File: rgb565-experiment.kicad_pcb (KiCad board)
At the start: 4 copper layers, 99.1 x 63.5 mm, 36 parts, among them J1 ST_SHIFTER_SOCKET, J2 Conn_01x02, SW1 SW_SPDT, U1 74HC00, U2 ST_SHIFTER, U3 ST_SHIFTER, U4 74HC245, U5 74LS257, U6 74HC245

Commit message: prepare next version
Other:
- board text added: "Original project : https://github.com/sporniket/atari-st-mod-rgb565-experiment v1.0.0-xprc3"
- board text removed: "Original project : https://github.com/sporniket/atari-st-mod-rgb565-experiment v1.0.0-xprc2"
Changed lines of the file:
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@@
   (page A4)
   (title_block
-    (title "Experimental RGB-565 mod for the Atari ST")
-    (date 2021-12-18)
-    (rev v1.0.0-xprc2)
+    (title "Experimental RGB-565 colorspace for the Atari ST")
+    (date 2021-12-24)
+    (rev v1.0.0-xprc3)
     (company Sporniket-Studio.com)
   )
@@
     (effects (font (size 1 1) (thickness 0.15)) (justify mirror))
   )
-  (gr_text "Original project : https://github.com/sporniket/atari-st-mod-rgb565-experiment v1.0.0-xprc2" (at 139.4206 132.0292) (layer F.SilkS)
+  (gr_text "Original project : https://github.com/sporniket/atari-st-mod-rgb565-experiment v1.0.0-xprc3" (at 139.4206 132.0292) (layer F.SilkS)
     (effects (font (size 1.016 1.016) (thickness 0.1524)))
   )

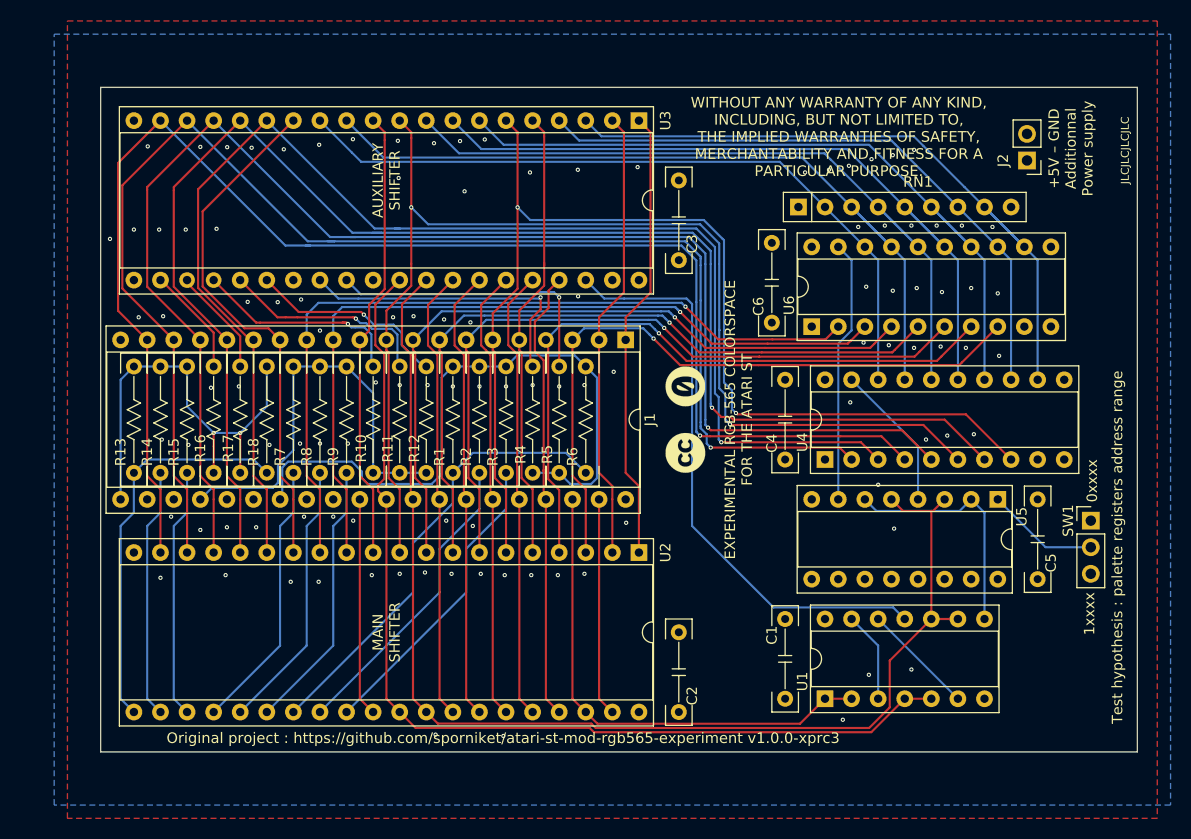
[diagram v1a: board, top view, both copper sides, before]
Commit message: Release Candidate 1 : modifications following experiments with the experimental version
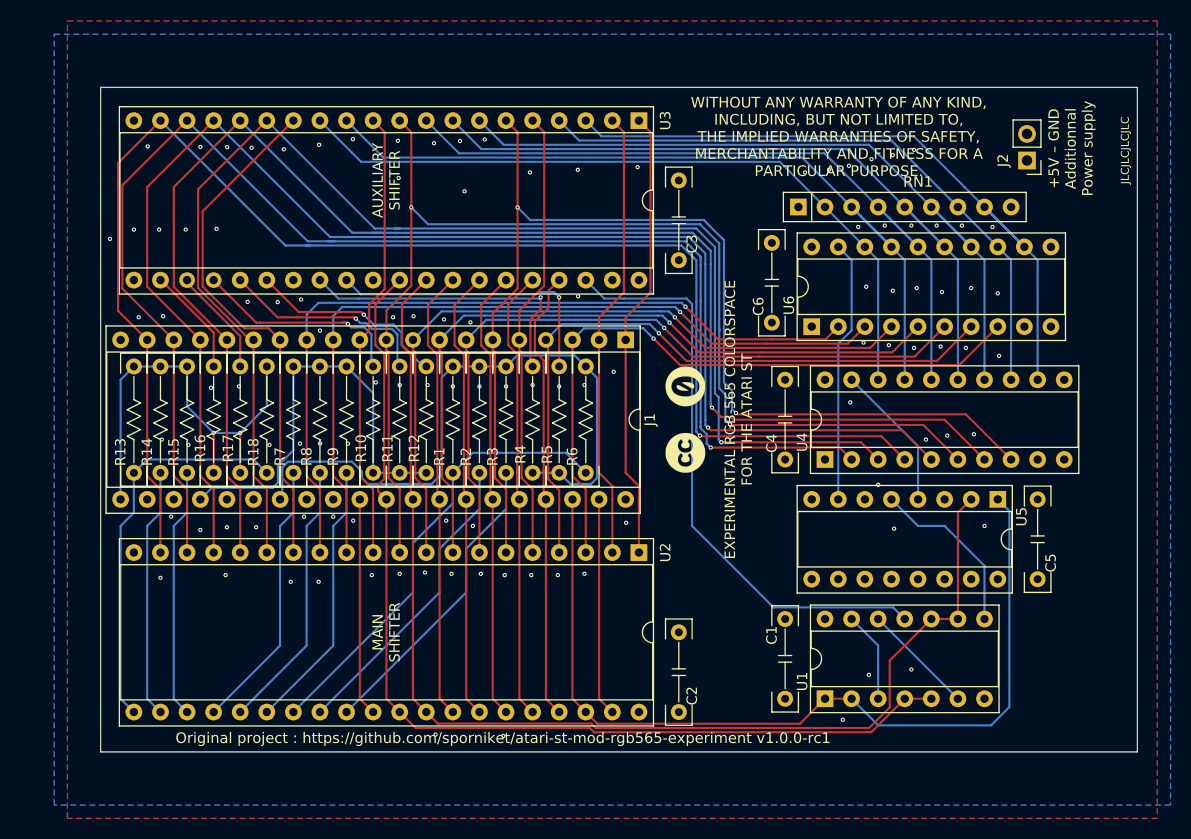
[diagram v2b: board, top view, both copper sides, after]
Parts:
- removed SW1: SW_SPDT, Connector_PinHeader_2.54mm:PinHeader_1x03_P2.54mm_Vertical
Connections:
- U5 pad 1: Net-(SW1-Pad2) -> /cs
- U5 pad 2: Net-(U1-Pad8) -> /a5
- U5 pad 3: /a5 -> +5V
- U5 pad 5: /a5 -> Net-(U1-Pad8)
- U5 pad 6: Net-(U1-Pad8) -> GND
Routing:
- net /cs: track 47.7 -> 84.9 mm
- net Net-(SW1-Pad2): track 10.8 -> 0.00 mm
- net Net-(U1-Pad8): track 23.0 -> 16.6 mm
- net /a5: track 117.9 -> 113.5 mm
- net GND: vias 108 -> 109
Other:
- board text added: "Original project : https://github.com/sporniket/atari-st-mod-rgb565-experiment v1.0.0-rc1"
- board text removed: "0xxxx"
- board text removed: "1xxxx"
- board text removed: "Original project : https://github.com/sporniket/atari-st-mod-rgb565-experiment v1.0.0-xprc3"
- board text removed: "Test hypothesis : palette registers address range"
